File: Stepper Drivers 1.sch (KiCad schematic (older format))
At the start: 88 parts

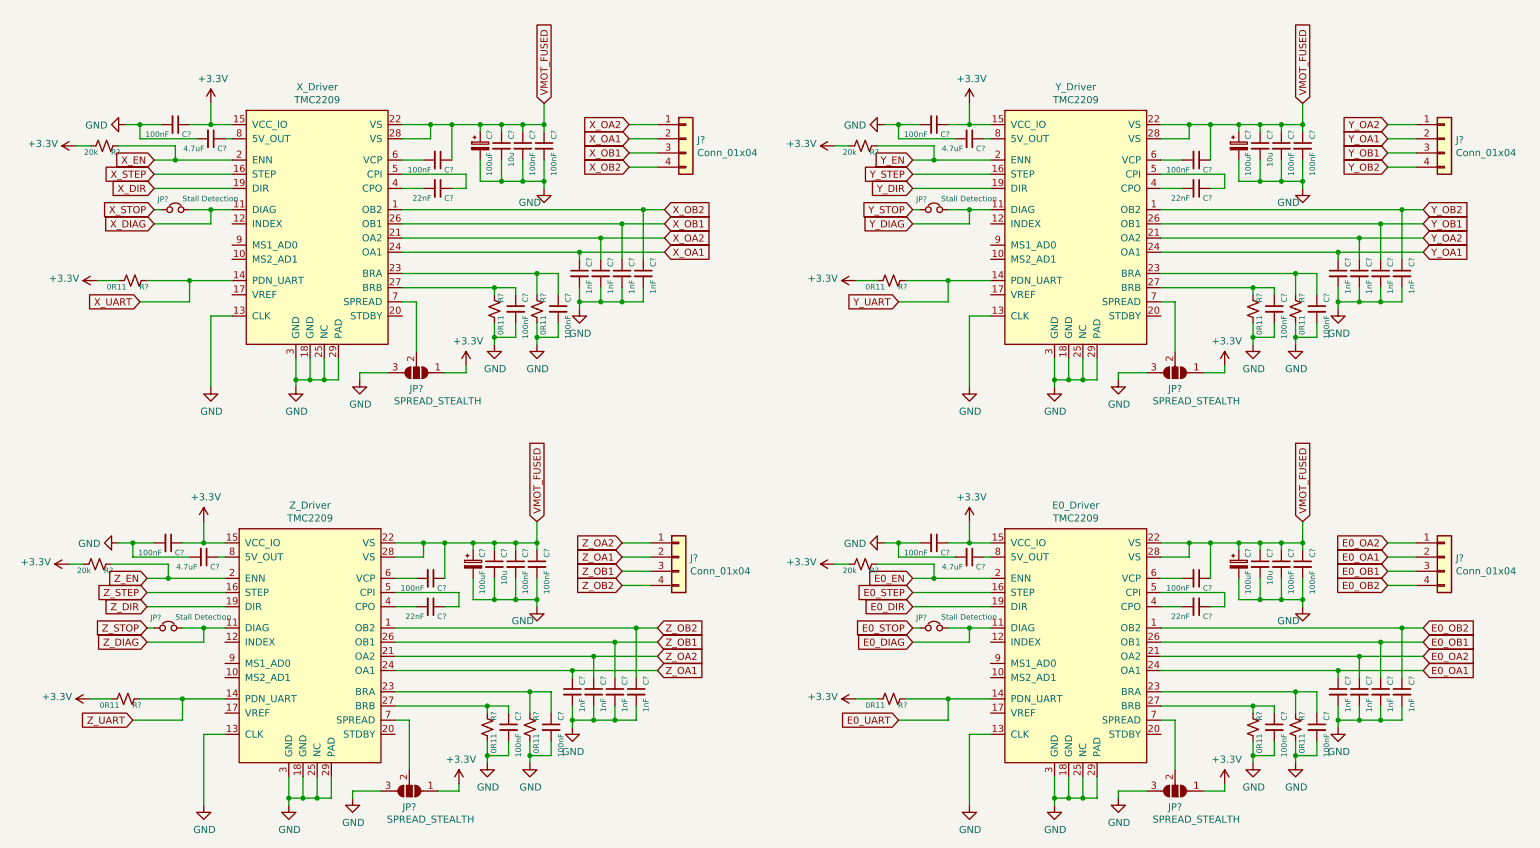
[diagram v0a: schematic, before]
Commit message: added resistor numbers
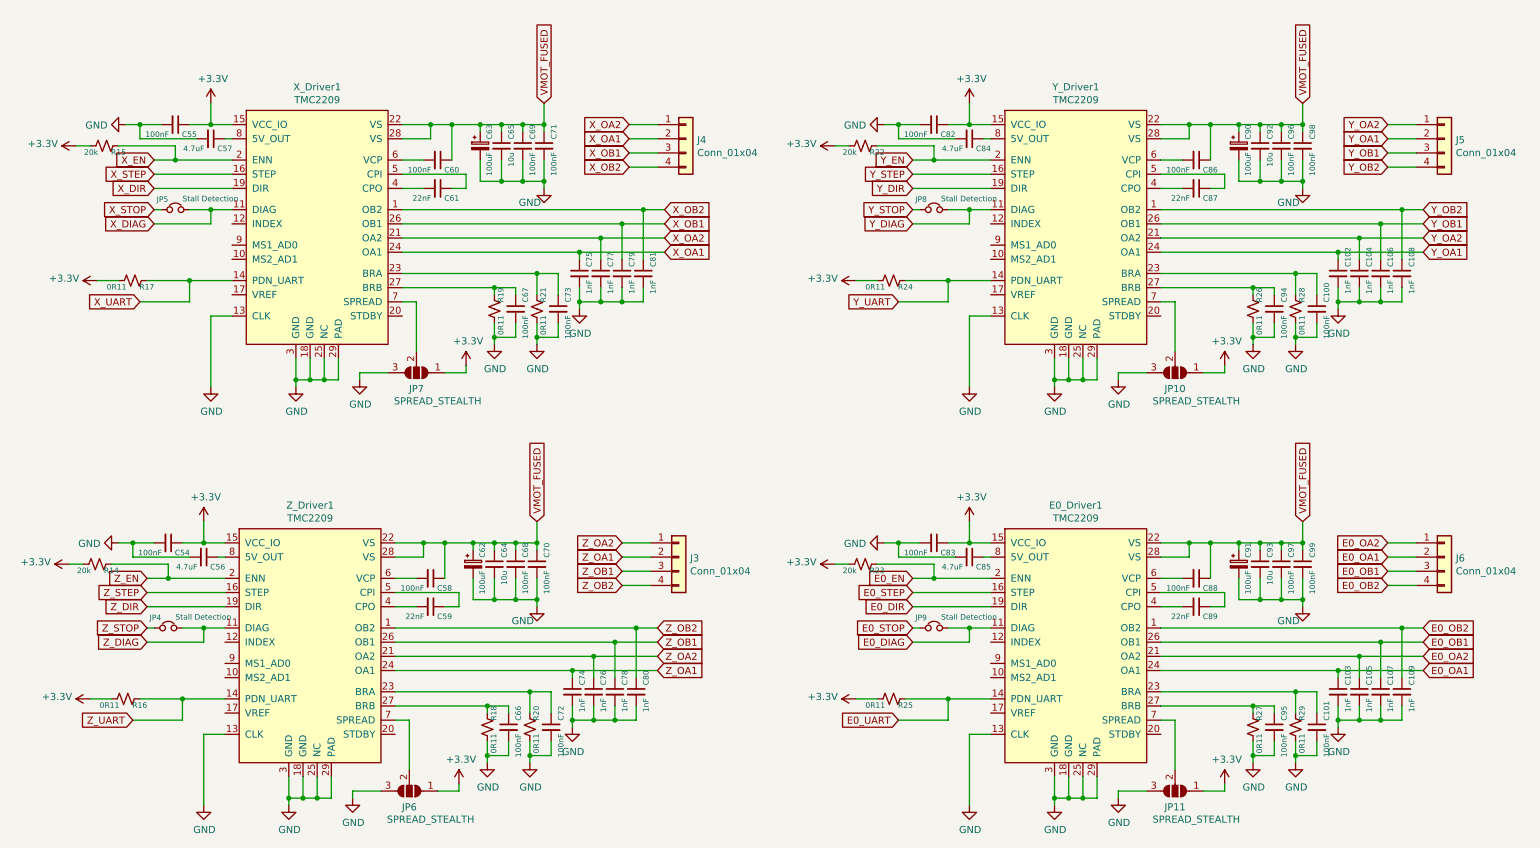
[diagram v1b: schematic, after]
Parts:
- gave numbers to parts that had none: 84
- renumbered E0_Driver to E0_Driver1, X_Driver to X_Driver1, Y_Driver to Y_Driver1, Z_Driver to Z_Driver1

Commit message: added raspberry pi header
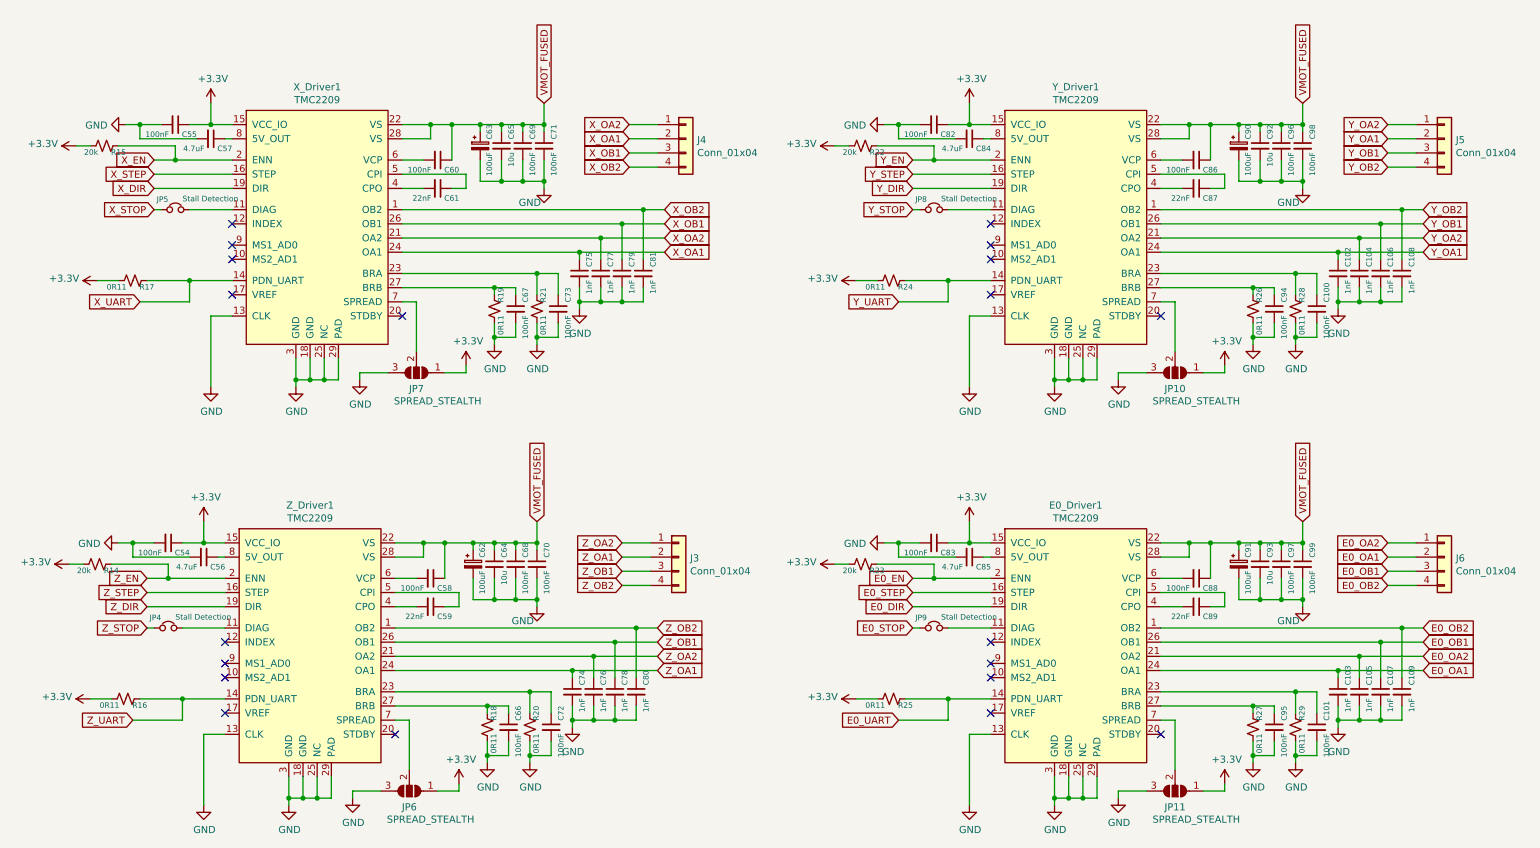
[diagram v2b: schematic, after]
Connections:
- net E0_DIAG: no longer names the net of E0_Driver1.11 (DIAG), JP9.2
- net X_DIAG: no longer names the net of JP5.2, X_Driver1.11 (DIAG)
- net Y_DIAG: no longer names the net of JP8.2, Y_Driver1.11 (DIAG)
- net Z_DIAG: no longer names the net of JP4.2, Z_Driver1.11 (DIAG)
- no-connect marks 0 -> 20
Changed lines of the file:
@@
 Text GLabel 1450 1800 0    50   Input ~ 0
 X_STOP
-Text GLabel 1450 1900 0    50   Input ~ 0
-X_DIAG
-Wire Wire Line
-	1450 1900 1850 1900
-Wire Wire Line
-	1850 1900 1850 1800
-Wire Wire Line
-	1850 1800 2000 1800
 Wire Wire Line
 	1450 1800 1500 1800
-Wire Wire Line
-	1700 1800 1850 1800
-Connection ~ 1850 1800
 Text GLabel 5050 1900 2    50   Input ~ 0
 X_OB1
@@
 $EndComp
 Wire Wire Line
-	6800 1900 7200 1900
-Wire Wire Line
-	7200 1900 7200 1800
-Wire Wire Line
-	7200 1800 7350 1800
-Wire Wire Line
 	6800 1800 6850 1800
-Wire Wire Line
-	7050 1800 7200 1800
-Connection ~ 7200 1800
 $Comp
 L Device:C_Small C102
@@
 $EndComp
 Wire Wire Line
-	1400 4850 1800 4850
-Wire Wire Line
-	1800 4850 1800 4750
-Wire Wire Line
-	1800 4750 1950 4750
-Wire Wire Line
 	1400 4750 1450 4750
-Wire Wire Line
-	1650 4750 1800 4750
-Connection ~ 1800 4750
 $Comp
 L Device:C_Small C74
@@
 $EndComp
 Wire Wire Line
-	6800 4850 7200 4850
-Wire Wire Line
-	7200 4850 7200 4750
-Wire Wire Line
-	7200 4750 7350 4750
-Wire Wire Line
 	6800 4750 6850 4750
-Wire Wire Line
-	7050 4750 7200 4750
-Connection ~ 7200 4750
 $Comp
 L Device:C_Small C103
@@
 Text GLabel 6800 1800 0    50   Input ~ 0
 Y_STOP
-Text GLabel 6800 1900 0    50   Input ~ 0
-Y_DIAG
 Text GLabel 6700 2450 0    50   Input ~ 0
 Y_UART
@@
 Text GLabel 1400 4750 0    50   Input ~ 0
 Z_STOP
-Text GLabel 1400 4850 0    50   Input ~ 0
-Z_DIAG
 $Comp
 L Jumper:SolderJumper_3_Open JP7
@@
 Text GLabel 6800 4750 0    50   Input ~ 0
 E0_STOP
-Text GLabel 6800 4850 0    50   Input ~ 0
-E0_DIAG
 Text GLabel 10400 4750 2    50   Input ~ 0
 E0_OB2
@@
 Text GLabel 1300 5400 0    50   Input ~ 0
 Z_UART
+NoConn ~ 2000 1900
+NoConn ~ 2000 2050
+NoConn ~ 2000 2150
+NoConn ~ 2000 2400
+NoConn ~ 7350 1900
+NoConn ~ 7350 2050
+NoConn ~ 7350 2150
+NoConn ~ 7350 2400
+NoConn ~ 1950 4850
+NoConn ~ 1950 5000
+NoConn ~ 1950 5100
+NoConn ~ 1950 5350
+NoConn ~ 7350 4850
+NoConn ~ 7350 5000
+NoConn ~ 7350 5100
+NoConn ~ 7350 5350
+NoConn ~ 8550 5500
+NoConn ~ 3150 5500
+NoConn ~ 3200 2550
+NoConn ~ 8550 2550
+Wire Wire Line
+	1650 4750 1950 4750
+Wire Wire Line
+	1700 1800 2000 1800
+Wire Wire Line
+	7050 1800 7350 1800
+Wire Wire Line
+	7050 4750 7350 4750
 $EndSCHEMATC

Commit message: assigned some footprints
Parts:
- C100, C101, C54, C55, C58, C60, C66, C67, C68, C69, C70, C71, C72, C73, C82, C83, C86, C88, C94, C95, C96, C97, C98, C99: footprint (none) -> Capacitor_SMD:C_0603_1608Metric_Pad1.05x0.95mm_HandSolder
- C62, C63, C90, C91: footprint (none) -> Capacitor_SMD:CP_Elec_6.3x7.7
- C64, C65, C92, C93: footprint (none) -> Capacitor_SMD:C_0805_2012Metric_Pad1.15x1.40mm_HandSolder
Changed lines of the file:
@@
 F 0 "C63" V 3838 1396 39  0000 L BNN
 F 1 "100uF" V 3838 1305 39  0000 R BNN
-F 2 "" H 3750 1350 50  0001 C CNN
+F 2 "Capacitor_SMD:CP_Elec_6.3x7.7" H 3750 1350 50  0001 C CNN
 F 3 "~" H 3750 1350 50  0001 C CNN
 	1    3750 1350
@@
 F 0 "C65" V 3992 1396 39  0000 L BNN
 F 1 "10u" V 3992 1305 39  0000 R BNN
-F 2 "" H 3900 1350 50  0001 C CNN
+F 2 "Capacitor_SMD:C_0805_2012Metric_Pad1.15x1.40mm_HandSolder" H 3900 1350 50  0001 C CNN
 F 3 "~" H 3900 1350 50  0001 C CNN
 	1    3900 1350
@@
 F 0 "C71" V 4292 1396 39  0000 L BNN
 F 1 "100nF" V 4292 1305 39  0000 R BNN
-F 2 "" H 4200 1350 50  0001 C CNN
+F 2 "Capacitor_SMD:C_0603_1608Metric_Pad1.05x0.95mm_HandSolder" H 4200 1350 50  0001 C CNN
 F 3 "~" H 4200 1350 50  0001 C CNN
 	1    4200 1350
@@
 F 0 "C69" V 4142 1396 39  0000 L BNN
 F 1 "100nF" V 4142 1305 39  0000 R BNN
-F 2 "" H 4050 1350 50  0001 C CNN
+F 2 "Capacitor_SMD:C_0603_1608Metric_Pad1.05x0.95mm_HandSolder" H 4050 1350 50  0001 C CNN
 F 3 "~" H 4050 1350 50  0001 C CNN
 	1    4050 1350
@@
 F 0 "C60" V 3542 1496 39  0000 L BNN
 F 1 "100nF" V 3542 1405 39  0000 R BNN
-F 2 "" H 3450 1450 50  0001 C CNN
+F 2 "Capacitor_SMD:C_0603_1608Metric_Pad1.05x0.95mm_HandSolder" H 3450 1450 50  0001 C CNN
 F 3 "~" H 3450 1450 50  0001 C CNN
 	1    3450 1450
@@
 F 0 "C55" V 1692 1246 39  0000 L BNN
 F 1 "100nF" V 1692 1155 39  0000 R BNN
-F 2 "" H 1600 1200 50  0001 C CNN
+F 2 "Capacitor_SMD:C_0603_1608Metric_Pad1.05x0.95mm_HandSolder" H 1600 1200 50  0001 C CNN
 F 3 "~" H 1600 1200 50  0001 C CNN
 	1    1600 1200
@@
 F 0 "C73" V 4392 2546 39  0000 L BNN
 F 1 "100nF" V 4392 2455 39  0000 R BNN
-F 2 "" H 4300 2500 50  0001 C CNN
+F 2 "Capacitor_SMD:C_0603_1608Metric_Pad1.05x0.95mm_HandSolder" H 4300 2500 50  0001 C CNN
 F 3 "~" H 4300 2500 50  0001 C CNN
 	1    4300 2500
@@
 F 0 "C67" V 4092 2546 39  0000 L BNN
 F 1 "100nF" V 4092 2455 39  0000 R BNN
-F 2 "" H 4000 2500 50  0001 C CNN
+F 2 "Capacitor_SMD:C_0603_1608Metric_Pad1.05x0.95mm_HandSolder" H 4000 2500 50  0001 C CNN
 F 3 "~" H 4000 2500 50  0001 C CNN
 	1    4000 2500
@@
 F 0 "C90" V 9188 1396 39  0000 L BNN
 F 1 "100uF" V 9188 1305 39  0000 R BNN
-F 2 "" H 9100 1350 50  0001 C CNN
+F 2 "Capacitor_SMD:CP_Elec_6.3x7.7" H 9100 1350 50  0001 C CNN
 F 3 "~" H 9100 1350 50  0001 C CNN
 	1    9100 1350
@@
 F 0 "C92" V 9342 1396 39  0000 L BNN
 F 1 "10u" V 9342 1305 39  0000 R BNN
-F 2 "" H 9250 1350 50  0001 C CNN
+F 2 "Capacitor_SMD:C_0805_2012Metric_Pad1.15x1.40mm_HandSolder" H 9250 1350 50  0001 C CNN
 F 3 "~" H 9250 1350 50  0001 C CNN
 	1    9250 1350
@@
 F 0 "C98" V 9642 1396 39  0000 L BNN
 F 1 "100nF" V 9642 1305 39  0000 R BNN
-F 2 "" H 9550 1350 50  0001 C CNN
+F 2 "Capacitor_SMD:C_0603_1608Metric_Pad1.05x0.95mm_HandSolder" H 9550 1350 50  0001 C CNN
 F 3 "~" H 9550 1350 50  0001 C CNN
 	1    9550 1350
@@
 F 0 "C96" V 9492 1396 39  0000 L BNN
 F 1 "100nF" V 9492 1305 39  0000 R BNN
-F 2 "" H 9400 1350 50  0001 C CNN
+F 2 "Capacitor_SMD:C_0603_1608Metric_Pad1.05x0.95mm_HandSolder" H 9400 1350 50  0001 C CNN
 F 3 "~" H 9400 1350 50  0001 C CNN
 	1    9400 1350
@@
 F 0 "C86" V 8892 1496 39  0000 L BNN
 F 1 "100nF" V 8892 1405 39  0000 R BNN
-F 2 "" H 8800 1450 50  0001 C CNN
+F 2 "Capacitor_SMD:C_0603_1608Metric_Pad1.05x0.95mm_HandSolder" H 8800 1450 50  0001 C CNN
 F 3 "~" H 8800 1450 50  0001 C CNN
 	1    8800 1450
@@
 F 0 "C82" V 7042 1246 39  0000 L BNN
 F 1 "100nF" V 7042 1155 39  0000 R BNN
-F 2 "" H 6950 1200 50  0001 C CNN
+F 2 "Capacitor_SMD:C_0603_1608Metric_Pad1.05x0.95mm_HandSolder" H 6950 1200 50  0001 C CNN
 F 3 "~" H 6950 1200 50  0001 C CNN
 	1    6950 1200
@@
 F 0 "C100" V 9742 2546 39  0000 L BNN
 F 1 "100nF" V 9742 2455 39  0000 R BNN
-F 2 "" H 9650 2500 50  0001 C CNN
+F 2 "Capacitor_SMD:C_0603_1608Metric_Pad1.05x0.95mm_HandSolder" H 9650 2500 50  0001 C CNN
 F 3 "~" H 9650 2500 50  0001 C CNN
 	1    9650 2500
@@
 F 0 "C94" V 9442 2546 39  0000 L BNN
 F 1 "100nF" V 9442 2455 39  0000 R BNN
-F 2 "" H 9350 2500 50  0001 C CNN
+F 2 "Capacitor_SMD:C_0603_1608Metric_Pad1.05x0.95mm_HandSolder" H 9350 2500 50  0001 C CNN
 F 3 "~" H 9350 2500 50  0001 C CNN
 	1    9350 2500
@@
 F 0 "C62" V 3788 4346 39  0000 L BNN
 F 1 "100uF" V 3788 4255 39  0000 R BNN
-F 2 "" H 3700 4300 50  0001 C CNN
+F 2 "Capacitor_SMD:CP_Elec_6.3x7.7" H 3700 4300 50  0001 C CNN
 F 3 "~" H 3700 4300 50  0001 C CNN
 	1    3700 4300
@@
 F 0 "C64" V 3942 4346 39  0000 L BNN
 F 1 "10u" V 3942 4255 39  0000 R BNN
-F 2 "" H 3850 4300 50  0001 C CNN
+F 2 "Capacitor_SMD:C_0805_2012Metric_Pad1.15x1.40mm_HandSolder" H 3850 4300 50  0001 C CNN
 F 3 "~" H 3850 4300 50  0001 C CNN
 	1    3850 4300
@@
 F 0 "C70" V 4242 4346 39  0000 L BNN
 F 1 "100nF" V 4242 4255 39  0000 R BNN
-F 2 "" H 4150 4300 50  0001 C CNN
+F 2 "Capacitor_SMD:C_0603_1608Metric_Pad1.05x0.95mm_HandSolder" H 4150 4300 50  0001 C CNN
 F 3 "~" H 4150 4300 50  0001 C CNN
 	1    4150 4300
@@
 F 0 "C68" V 4092 4346 39  0000 L BNN
 F 1 "100nF" V 4092 4255 39  0000 R BNN
-F 2 "" H 4000 4300 50  0001 C CNN
+F 2 "Capacitor_SMD:C_0603_1608Metric_Pad1.05x0.95mm_HandSolder" H 4000 4300 50  0001 C CNN
 F 3 "~" H 4000 4300 50  0001 C CNN
 	1    4000 4300
@@
 F 0 "C58" V 3492 4446 39  0000 L BNN
 F 1 "100nF" V 3492 4355 39  0000 R BNN
-F 2 "" H 3400 4400 50  0001 C CNN
+F 2 "Capacitor_SMD:C_0603_1608Metric_Pad1.05x0.95mm_HandSolder" H 3400 4400 50  0001 C CNN
 F 3 "~" H 3400 4400 50  0001 C CNN
 	1    3400 4400
@@
 F 0 "C54" V 1642 4196 39  0000 L BNN
 F 1 "100nF" V 1642 4105 39  0000 R BNN
-F 2 "" H 1550 4150 50  0001 C CNN
+F 2 "Capacitor_SMD:C_0603_1608Metric_Pad1.05x0.95mm_HandSolder" H 1550 4150 50  0001 C CNN
 F 3 "~" H 1550 4150 50  0001 C CNN
 	1    1550 4150
@@
 F 0 "C72" V 4342 5496 39  0000 L BNN
 F 1 "100nF" V 4342 5405 39  0000 R BNN
-F 2 "" H 4250 5450 50  0001 C CNN
+F 2 "Capacitor_SMD:C_0603_1608Metric_Pad1.05x0.95mm_HandSolder" H 4250 5450 50  0001 C CNN
 F 3 "~" H 4250 5450 50  0001 C CNN
 	1    4250 5450
@@
 F 0 "C66" V 4042 5496 39  0000 L BNN
 F 1 "100nF" V 4042 5405 39  0000 R BNN
-F 2 "" H 3950 5450 50  0001 C CNN
+F 2 "Capacitor_SMD:C_0603_1608Metric_Pad1.05x0.95mm_HandSolder" H 3950 5450 50  0001 C CNN
 F 3 "~" H 3950 5450 50  0001 C CNN
 	1    3950 5450
@@
 F 0 "C91" V 9188 4346 39  0000 L BNN
 F 1 "100uF" V 9188 4255 39  0000 R BNN
-F 2 "" H 9100 4300 50  0001 C CNN
+F 2 "Capacitor_SMD:CP_Elec_6.3x7.7" H 9100 4300 50  0001 C CNN
 F 3 "~" H 9100 4300 50  0001 C CNN
 	1    9100 4300
@@
 F 0 "C93" V 9342 4346 39  0000 L BNN
 F 1 "10u" V 9342 4255 39  0000 R BNN
-F 2 "" H 9250 4300 50  0001 C CNN
+F 2 "Capacitor_SMD:C_0805_2012Metric_Pad1.15x1.40mm_HandSolder" H 9250 4300 50  0001 C CNN
 F 3 "~" H 9250 4300 50  0001 C CNN
 	1    9250 4300
@@
 F 0 "C99" V 9642 4346 39  0000 L BNN
 F 1 "100nF" V 9642 4255 39  0000 R BNN
-F 2 "" H 9550 4300 50  0001 C CNN
+F 2 "Capacitor_SMD:C_0603_1608Metric_Pad1.05x0.95mm_HandSolder" H 9550 4300 50  0001 C CNN
 F 3 "~" H 9550 4300 50  0001 C CNN
 	1    9550 4300
@@
 F 0 "C97" V 9492 4346 39  0000 L BNN
 F 1 "100nF" V 9492 4255 39  0000 R BNN
-F 2 "" H 9400 4300 50  0001 C CNN
+F 2 "Capacitor_SMD:C_0603_1608Metric_Pad1.05x0.95mm_HandSolder" H 9400 4300 50  0001 C CNN
 F 3 "~" H 9400 4300 50  0001 C CNN
 	1    9400 4300
@@
 F 0 "C88" V 8892 4446 39  0000 L BNN
 F 1 "100nF" V 8892 4355 39  0000 R BNN
-F 2 "" H 8800 4400 50  0001 C CNN
+F 2 "Capacitor_SMD:C_0603_1608Metric_Pad1.05x0.95mm_HandSolder" H 8800 4400 50  0001 C CNN
 F 3 "~" H 8800 4400 50  0001 C CNN
 	1    8800 4400
@@
 F 0 "C83" V 7042 4196 39  0000 L BNN
 F 1 "100nF" V 7042 4105 39  0000 R BNN
-F 2 "" H 6950 4150 50  0001 C CNN
+F 2 "Capacitor_SMD:C_0603_1608Metric_Pad1.05x0.95mm_HandSolder" H 6950 4150 50  0001 C CNN
 F 3 "~" H 6950 4150 50  0001 C CNN
 	1    6950 4150
@@
 F 0 "C101" V 9742 5496 39  0000 L BNN
 F 1 "100nF" V 9742 5405 39  0000 R BNN
-F 2 "" H 9650 5450 50  0001 C CNN
+F 2 "Capacitor_SMD:C_0603_1608Metric_Pad1.05x0.95mm_HandSolder" H 9650 5450 50  0001 C CNN
 F 3 "~" H 9650 5450 50  0001 C CNN
 	1    9650 5450
@@
 F 0 "C95" V 9442 5496 39  0000 L BNN
 F 1 "100nF" V 9442 5405 39  0000 R BNN
-F 2 "" H 9350 5450 50  0001 C CNN
+F 2 "Capacitor_SMD:C_0603_1608Metric_Pad1.05x0.95mm_HandSolder" H 9350 5450 50  0001 C CNN
 F 3 "~" H 9350 5450 50  0001 C CNN
 	1    9350 5450
